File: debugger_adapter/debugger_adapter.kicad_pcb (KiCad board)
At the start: 2 copper layers, 13 parts, among them X1 FT_CONN0_TAG, X10 FT_CONN_BREAKOUT, X11 DUT_CONN0_BREAKOUT, X12 VCC_SEL_UART, X13 DUT_CONN1_BREAKOUT, X2 FT_CONN1_TAG, X3 TAG_CONN_TAG, X4 FT_CONN_JTAG, X5 DUT_CONN_JTAG, X6 VCC_SEL_TAG, X7 VCC_SEL_JTAG, X8 FT_CONN_UART, X9 DUT_CONN_UART

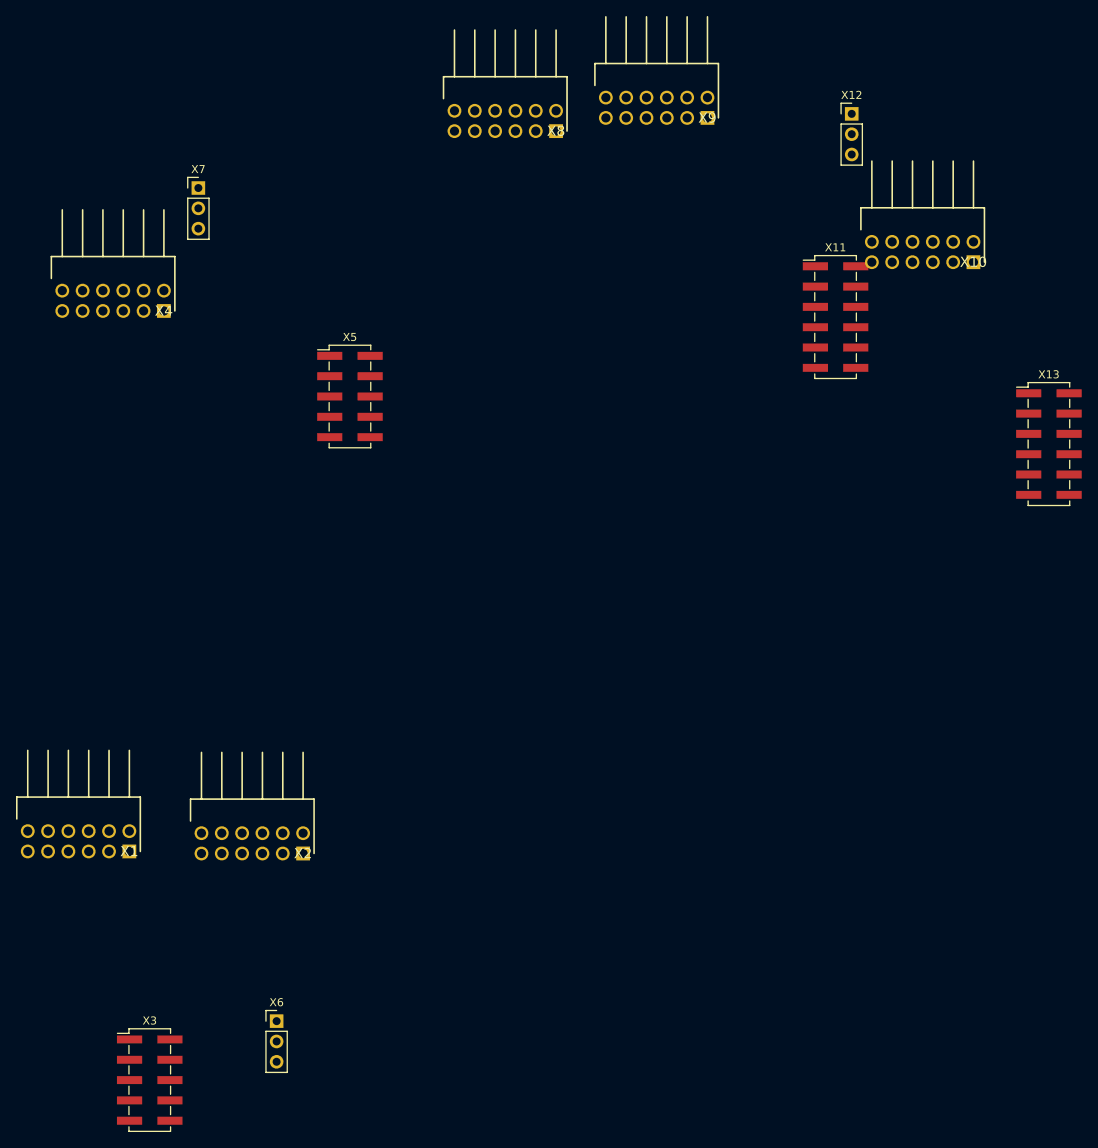
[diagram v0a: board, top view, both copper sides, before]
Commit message: decrease clearance of copper pours
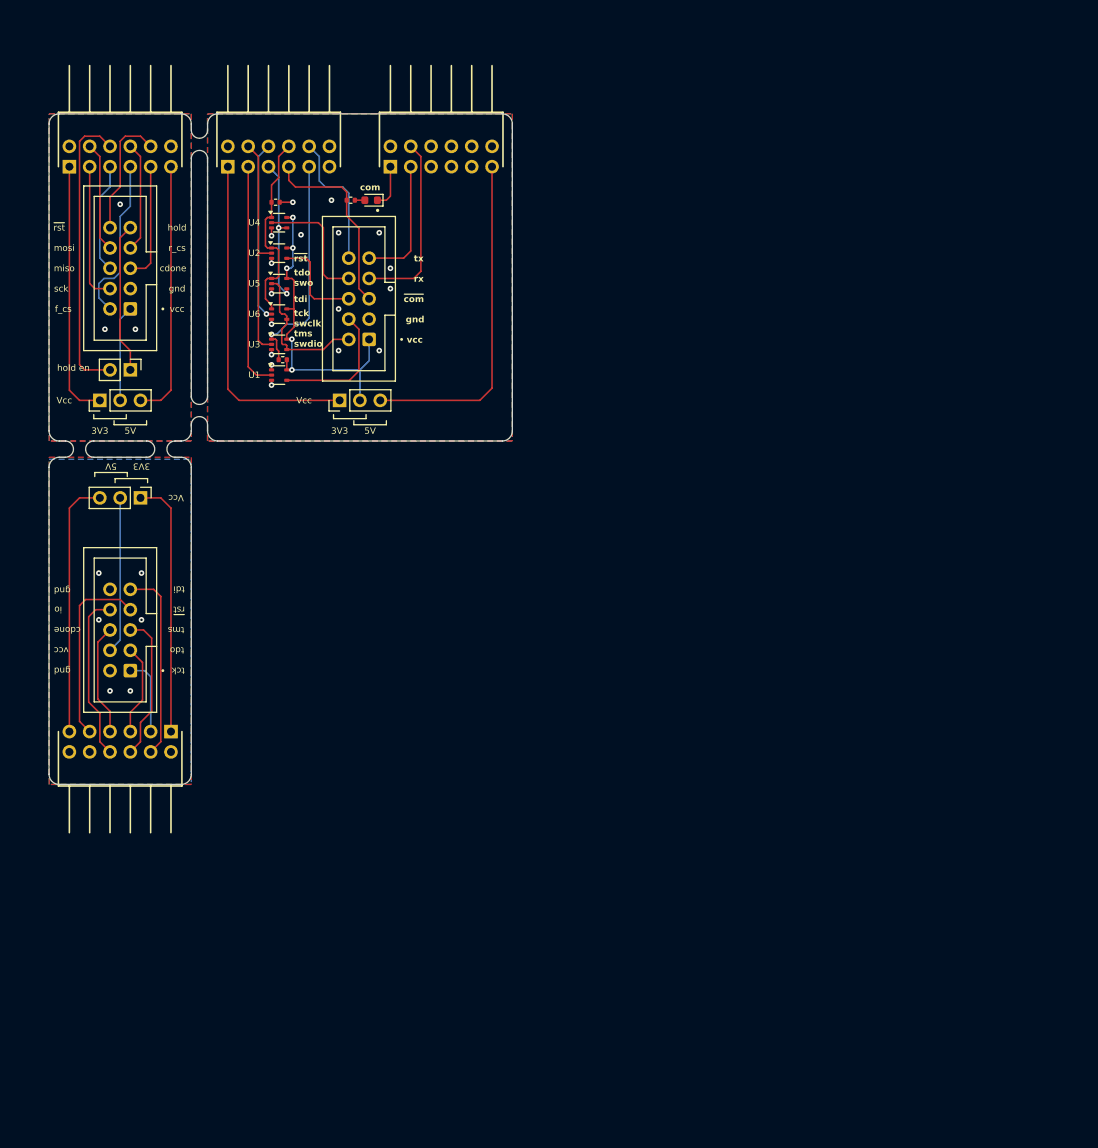
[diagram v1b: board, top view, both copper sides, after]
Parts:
- removed X11: DUT_CONN0_BREAKOUT, Connector_PinHeader_2.54mm:PinHeader_2x06_P2.54mm_Vertical_SMD
- removed X12: VCC_SEL_UART, Connector_PinHeader_2.54mm:PinHeader_1x03_P2.54mm_Vertical
- removed X13: DUT_CONN1_BREAKOUT, Connector_PinHeader_2.54mm:PinHeader_2x06_P2.54mm_Vertical_SMD
- added D1: LED_Comm, LED_SMD:LED_0603_1608Metric, F.Cu at (93.6, 63.9)
- added JP1: Jumper_2_Small_Open, Connector_PinHeader_2.54mm:PinHeader_1x02_P2.54mm_Vertical, F.Cu at (63.5, 85.1)
- added R2: 10k, Resistor_SMD:R_0402_1005Metric, F.Cu at (81.7, 64.1)
- added R3: 10k, Resistor_SMD:R_0402_1005Metric, F.Cu at (82.5, 83.8)
- added R4: 10k, Resistor_SMD:R_0402_1005Metric, F.Cu at (91.1, 63.9)
- added U1: 74LVC1G125, Package_TO_SOT_SMD:SOT-353_SC-70-5, F.Cu at (82.1, 85.7)
- added U2: 74LVC1G125, Package_TO_SOT_SMD:SOT-353_SC-70-5, F.Cu at (82.1, 70.5)
- added U3: 74LVC1G125, Package_TO_SOT_SMD:SOT-353_SC-70-5, F.Cu at (82.1, 81.9)
- added U4: 74LVC1G125, Package_TO_SOT_SMD:SOT-353_SC-70-5, F.Cu at (82.1, 66.7)
- added U5: 74LVC1G126, Package_TO_SOT_SMD:SOT-353_SC-70-5, F.Cu at (82.1, 74.3)
- added U6: 74LVC1G125, Package_TO_SOT_SMD:SOT-353_SC-70-5, F.Cu at (82.1, 78.1)
- X1: value FT_CONN0_TAG -> CONN_ICE40; footprint ft4232_debugger:header_male_02x06_HDRRA12W67P254_2X6_1524X254X503P -> Connector_IDC:IDC-Header_2x05_P2.54mm_Vertical
- X10: value FT_CONN_BREAKOUT -> VCC_SEL_TAG; footprint ft4232_debugger:header_male_02x06_HDRRA12W67P254_2X6_1524X254X503P -> Connector_PinHeader_2.54mm:PinHeader_1x03_P2.54mm_Vertical
- X2: value FT_CONN1_TAG -> FT_CONN_ICE40
- X3: value TAG_CONN_TAG -> CONN_ZYNQ; footprint Connector_PinHeader_2.54mm:PinHeader_2x05_P2.54mm_Vertical_SMD -> Connector_IDC:IDC-Header_2x05_P2.54mm_Vertical
- X4: value FT_CONN_JTAG -> FT_CONN_ZYNQ
- X5: value DUT_CONN_JTAG -> VCC_SEL_TAG; footprint Connector_PinHeader_2.54mm:PinHeader_2x05_P2.54mm_Vertical_SMD -> Connector_PinHeader_2.54mm:PinHeader_1x03_P2.54mm_Vertical
- X7: value VCC_SEL_JTAG -> FT_CONN_DEBUG_CHAN_0; footprint Connector_PinHeader_2.54mm:PinHeader_1x03_P2.54mm_Vertical -> ft4232_debugger:header_male_02x06_HDRRA12W67P254_2X6_1524X254X503P
- X8: value FT_CONN_UART -> FT_CONN_DEBUG_CHAN_1
- X9: value DUT_CONN_UART -> CONN_DEBUG; footprint ft4232_debugger:header_male_02x06_HDRRA12W67P254_2X6_1524X254X503P -> Connector_IDC:IDC-Header_2x05_P2.54mm_Vertical
- moved X2 90.7 mm to (55.9, 59.7)
- moved X10 81.1 mm to (89.7, 88.9), turned to 90 degrees
- moved X1 67.8 mm to (63.5, 77.5), turned to 180 degrees
- moved X6 67.6 mm to (64.8, 101.1), turned to -90 degrees
- moved X4 52.6 mm to (68.6, 130.3), turned to 180 degrees
- moved X3 51.2 mm to (63.5, 122.7), turned to 180 degrees
- moved X9 50.6 mm to (93.3, 81.3), turned to 180 degrees
- moved X5 31.3 mm to (59.7, 88.9), turned to 90 degrees
- moved X8 21.2 mm to (96.0, 59.7)
- moved X7 4.55 mm to (75.7, 59.7)
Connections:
- X1 pad 1: /TAG_CONN_3V3 -> /ice40_vcc
- X1 pad 10: unconnected-(X1-Pin_10-Pad10) -> /ice40_rst
- X1 pad 2: /TAG_CONN_GND -> /ice40_flash_cs
- X1 pad 3: /TAG_CONN_SCK -> /ice40_gnd
- X1 pad 4: /TAG_CONN_MOSI -> /ice40_sck
- X1 pad 5: /TAG_CONN_MISO -> /ice40_cdone
- X1 pad 6: /TAG_CONN_CS -> /ice40_si
- X1 pad 7: /TAG_CONN_IO0 -> /ice40_ram_cs
- X1 pad 8: /TAG_CONN_RST -> /ice40_so
- X1 pad 9: unconnected-(X1-Pin_9-Pad9) -> /ice40_hold
- X10 pad 1: /Breakout_3V3 -> /dbg_3v3
- X10 pad 2: /Breakout_GND -> /dbg_vcc
- X10 pad 3: /Breakout_xDBUS0 -> /dbg_5v
- X2 pad 1: /TAG_CONN_3V3 -> /ice40_3v3
- X2 pad 10: unconnected-(X2-Pin_10-Pad10) -> /ice40_rst
- X2 pad 11: /TAG_CONN_5V -> /ice40_5v
- X2 pad 12: /TAG_CONN_GND -> /ice40_gnd
- X2 pad 2: /TAG_CONN_GND -> /ice40_gnd
- X2 pad 3: /TAG_CONN_TX -> /ice40_sck
- X2 pad 4: /TAG_CONN_RX -> /ice40_so
- X2 pad 5: unconnected-(X2-Pin_5-Pad5) -> /ice40_si
- X2 pad 6: unconnected-(X2-Pin_6-Pad6) -> Net-(JP1-B)
- X2 pad 7: unconnected-(X2-Pin_7-Pad7) -> /ice40_flash_cs
- X2 pad 8: unconnected-(X2-Pin_8-Pad8) -> /ice40_ram_cs
- X2 pad 9: unconnected-(X2-Pin_9-Pad9) -> /ice40_cdone
- X3 pad 1: /TAG_CONN_VCC -> /zynq_tck
- X3 pad 10: /TAG_CONN_RST -> /zynq_gnd
- X3 pad 2: /TAG_CONN_CS -> /zynq_gnd
- X3 pad 3: /TAG_CONN_GND -> /zynq_tdo
- X3 pad 4: /TAG_CONN_SCK -> /zynq_vcc
- X3 pad 5: /TAG_CONN_IO0 -> /zynq_tms
- X3 pad 6: /TAG_CONN_MOSI -> /zynq_cdone
- X3 pad 7: /TAG_CONN_RX -> /zynq_rst
- X3 pad 8: /TAG_CONN_MISO -> /zynq_io
- X3 pad 9: /TAG_CONN_TX -> /zynq_tdi
- X4 pad 1: /IDC_02x05_3V3 -> /zynq_3v3
- X4 pad 11: /IDC_02x05_5V -> /zynq_5v
- X4 pad 12: /IDC_02x05_GND -> /zynq_gnd
- X4 pad 2: /IDC_02x05_GND -> /zynq_gnd
- X4 pad 3: /IDC_02x05_TCK -> /zynq_tck
- X4 pad 4: /IDC_02x05_TDI -> /zynq_tdi
- X4 pad 5: /IDC_02x05_TDO -> /zynq_tdo
- X4 pad 6: /IDC_02x05_TMS -> /zynq_tms
- X4 pad 7: unconnected-(X4-Pin_7-Pad7) -> /zynq_cdone
- X4 pad 8: /IDC_02x05_RST -> /zynq_io
- X4 pad 9: unconnected-(X4-Pin_9-Pad9) -> /zynq_rst
- X5 pad 1: /IDC_02x05_VCC -> /ice40_3v3
- X5 pad 2: /IDC_02x05_TMS -> /ice40_vcc
- X5 pad 3: /IDC_02x05_GND -> /ice40_5v
- X6 pad 1: /TAG_CONN_3V3 -> /zynq_3v3
- X6 pad 2: /TAG_CONN_VCC -> /zynq_vcc
- X6 pad 3: /TAG_CONN_5V -> /zynq_5v
- X7 pad 1: /IDC_02x05_3V3 -> /dbg_3v3
- X7 pad 2: /IDC_02x05_VCC -> /dbg_gnd
- X7 pad 3: /IDC_02x05_5V -> /dbg_ft_tck_swclk
- X8 pad 1: /IDC_02x03_3V3 -> /dbg_3v3_led
- X8 pad 11: /IDC_02x03_5V -> /dbg_5v
- X8 pad 12: /IDC_02x03_GND -> /dbg_gnd
- X8 pad 2: /IDC_02x03_GND -> /dbg_gnd
- X8 pad 3: /IDC_02x03_TXD -> /dbg_tx
- X8 pad 4: /IDC_02x03_RXD -> /dbg_rx
- X9 pad 1: unconnected-(X9-Pin_1-Pad1) -> /dbg_vcc
- X9 pad 10: (no net) -> /dbg_rst
- X9 pad 2: /IDC_02x03_VCC -> /dbg_tms_swdio
- X9 pad 3: /IDC_02x03_RXD -> /dbg_gnd
- X9 pad 4: /IDC_02x03_GND -> /dbg_tck_swclk
- X9 pad 5: /IDC_02x03_TXD -> /~{dbg_com}
- X9 pad 6: unconnected-(X9-Pin_6-Pad6) -> /dbg_tdi
- X9 pad 7: (no net) -> /dbg_rx
- X9 pad 8: (no net) -> /dbg_tdo_swo
- X9 pad 9: (no net) -> /dbg_tx
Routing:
- net /dbg_vcc: track 0.00 -> 42.4 mm, vias 0 -> 5
- net /dbg_3v3: track 0.00 -> 42.4 mm
- net /dbg_5v: track 0.00 -> 42.3 mm
- net Net-(JP1-B): track 0.00 -> 36.6 mm
- net /ice40_5v: track 0.00 -> 32.3 mm
- net /zynq_3v3: track 0.00 -> 32.3 mm
- net /ice40_3v3: track 0.00 -> 32.3 mm
- net /zynq_5v: track 0.00 -> 32.3 mm
- net /dbg_ft_tck_swclk: track 0.00 -> 28.4 mm
- net /dbg_ft_tdi: track 0.00 -> 28.3 mm
- net /~{dbg_ft_swdio_oe}: track 0.00 -> 28.3 mm, vias 0 -> 1
- net /dbg_swd_en: track 0.00 -> 24.8 mm
- net /zynq_tdi: track 0.00 -> 24.1 mm
- net /~{dbg_com}: track 0.00 -> 24.1 mm
- net /zynq_rst: track 0.00 -> 23.5 mm
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- added copper zone on B.Cu, net /dbg_gnd
- added copper zone on F.Cu, net /dbg_gnd
- added copper zone on B.Cu, net /ice40_gnd
- added copper zone on F.Cu, net /ice40_gnd
- added copper zone on B.Cu, net /zynq_gnd
- added copper zone on F.Cu, net /zynq_gnd
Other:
- board outline added: 57.9 x 83.8 mm
- board text added: "3V3"
- board text added: "5V"
- board text added: "ICE40 FPGA debug adapter"
- board text added: "Vcc"
- board text added: "ZYNQ SoC debug adapter"
- board text added: "cdone"
- board text added: "com"
- board text added: "f_cs"
- board text added: "f_cs xD4"
- board text added: "general purpose debug adapter JTAG/SWD & UART"
- board text added: "gnd"
- board text added: "hold"
- board text added: "hold en"
- board text added: "io"
- board text added: "miso"
- board text added: "mosi"
- board text added: "r_cs"
- board text added: "rst xD6"
- board text added: "rx"
- board text added: "sck"
- board text added: "sck xD0"
- board text added: "si xD2"
- board text added: "so xD1"
- board text added: "tck"
- board text added: "tck swclk"
- board text added: "tck xD0"
- board text added: "tck xD0 swclk"
- board text added: "tdi"
- board text added: "tdi xD1"
- board text added: "tdo"
- board text added: "tdo swo"
- board text added: "tdo xD2"
- board text added: "tdo xD2 swo"
- board text added: "tms"
- board text added: "tms swdio"
- board text added: "tms xD3"
- board text added: "tms xD3 swdio"
- board text added: "tx"
- board text added: "vcc"
- board text added: "xD0 tx"
- board text added: "xD1 rx"
- board text added: "xD3 hold"
- board text added: "xD4 done"
- board text added: "xD4 ~{com}"
- board text added: "xD5 io"
- board text added: "xD5 r_cs"
- board text added: "xD6 done"
- board text added: "~{com}"
- board text added: "~{rst}"
- board text added: "~{rst} xD7"
